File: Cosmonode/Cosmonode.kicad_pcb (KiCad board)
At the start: 2 copper layers, 59.7 x 34.9 mm, 30 parts, among them J1 CONN_01X07, J2 CONN_01X07, J3 CONN_01X02, J4 CONN_01X01, J5 CONN_01X06, SW1 SW_DIP_x01, U1 ATMEGA328P-AU, U2 RFM69CW, U3 M25P40, U4 XC6206P332MR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

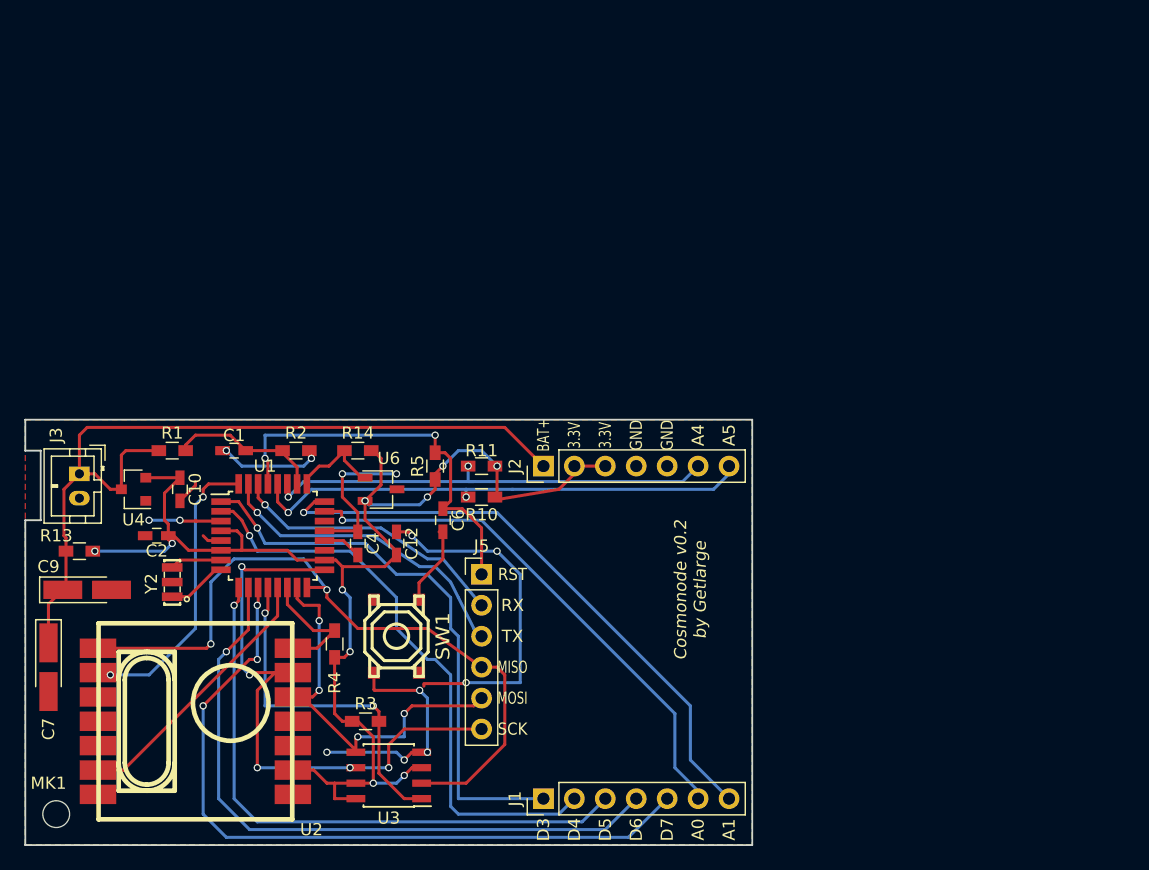
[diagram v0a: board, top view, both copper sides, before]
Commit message: new version 0.3
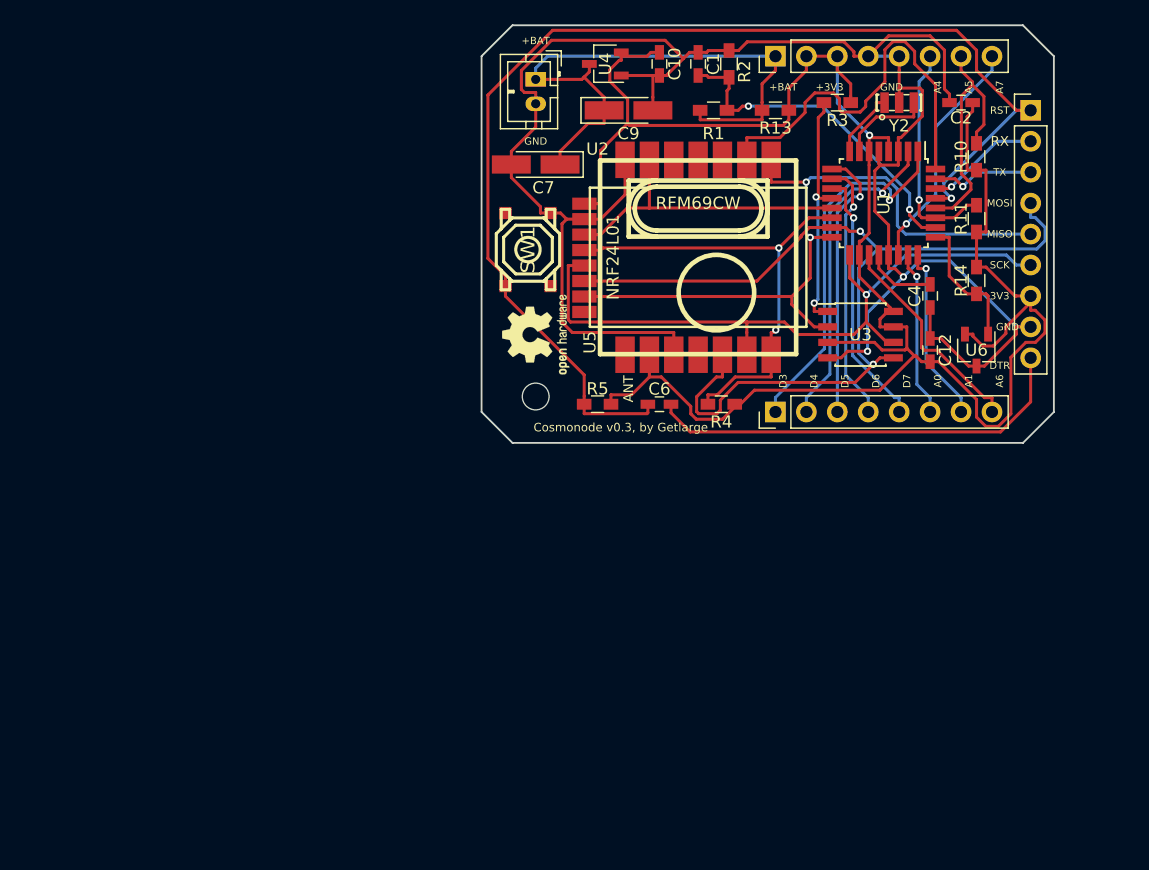
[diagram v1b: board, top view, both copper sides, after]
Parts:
- added U5: NRF24L01, mysensors_radios:NRF24L01-SMD, F.Cu at (163.2, 96.5)
- J1, J2: value CONN_01X07 -> CONN_01X08; footprint Socket_Strips:Socket_Strip_Straight_1x07_Pitch2.54mm -> Pin_Headers:Pin_Header_Straight_1x08_Pitch2.54mm
- J4: moved to F.Cu
- J5: value CONN_01X06 -> CONN_01X09; footprint Pin_Headers:Pin_Header_Straight_1x06_Pitch2.54mm -> Pin_Headers:Pin_Header_Straight_1x09_Pitch2.54mm
- U4: footprint TO_SOT_Packages_SMD:SOT-23 -> TO_SOT_Packages_SMD:TSOT-23
- moved C2 75.0 mm to (185.4, 83.8)
- moved Y2 71.5 mm to (180.3, 83.8), turned to 0 degrees
- moved R13 67.6 mm to (170.2, 84.5)
- moved R3 63.9 mm to (175.3, 83.8), turned to 180 degrees
- moved C9 59.4 mm to (158.1, 84.5)
- moved J5 59.0 mm to (191.1, 84.5)
- moved C7 57.5 mm to (150.5, 88.9), turned to 180 degrees
- moved U1 57.1 mm to (179.1, 92.1), turned to 270 degrees
- moved U2 56.2 mm to (163.8, 96.5), turned to 270 degrees
- moved U3 53.0 mm to (177.2, 102.9), turned to 0 degrees
- moved R14 52.7 mm to (186.7, 98.4), turned to 90 degrees
- moved C10 52.6 mm to (160.7, 80.6)
- moved R1 52.5 mm to (165.1, 84.5)
- moved MK1 52.2 mm to (150.5, 108.0)
- moved U4 52.2 mm to (156.2, 80.6)
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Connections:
- J5 pad 4: /MISO -> /MOSI
- J5 pad 5: /MOSI -> /MISO
- SW1 pad 2: /DTR -> /RST
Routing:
- net GND: track 79.8 -> 163.5 mm, vias 13 -> 2
- net /RST: track 33.0 -> 98.3 mm, vias 2 -> 1
- net +3V3: track 112.8 -> 170.1 mm, vias 10 -> 1
- net /MOSI: track 33.4 -> 79.7 mm, vias 4 -> 2
- net /D7: track 61.1 -> 21.6 mm, vias 3 -> 1
- net /A1: track 49.3 -> 14.8 mm
- net /D6: track 54.7 -> 21.6 mm
- net /A0: track 43.8 -> 13.7 mm
- net /DTR: track 6.70 -> 35.5 mm
- net /D10: track 10.2 -> 39.0 mm, vias 0 -> 2
- net /D5: track 49.6 -> 22.7 mm
- net /D4: track 48.8 -> 26.8 mm
- net /A5: track 41.8 -> 21.0 mm, vias 2 -> 0
- net /BAT+: track 67.9 -> 48.0 mm
- net /A7: track 0.00 -> 19.5 mm, vias 0 -> 1
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- removed copper zone on F.Cu, net GND
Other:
- board size 59.7 x 34.9 mm -> 47 x 34.3 mm
- board text added: "+3V3"
- board text added: "+BAT"
- board text added: "3V3"
- board text added: "A6"
- board text added: "A7"
- board text added: "ANT"
- board text added: "Cosmonode v0.3, by Getlarge"
- board text added: "DTR"
- board text added: "Do it yourself and do your best"
- board text removed: "3.3V"
- board text removed: "BAT+"
- board text removed: "Cosmonode v0.2 by Getlarge"

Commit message: big push!
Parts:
- removed C10: 4.7uF, Capacitors_SMD:C_0603_HandSoldering
- removed C12: 100nF, Capacitors_SMD:C_0603_HandSoldering
- removed C9: 47uF, Capacitors_Tantalum_SMD:CP_Tantalum_Case-A_EIA-3216-18_Hand
- removed R10, R11: 1k, Resistors_SMD:R_0603_HandSoldering
- removed R13: 0, Resistors_SMD:R_0603_HandSoldering
- removed R14: 100k, Resistors_SMD:R_0603_HandSoldering
- removed Y2: Crystal_GND2, SMD-RESONATOR-8MHZ-33PF-0.1__3P-3.2X1.3MM_:X3-SMD-3.6X1.3X0.8MM
- added C3: 100nF, Capacitors_SMD:C_0603_HandSoldering, F.Cu at (183.5, 100.3)
- added C5: 47uF, Capacitors_Tantalum_SMD:CP_Tantalum_Case-A_EIA-3216-18_Hand, F.Cu at (158.1, 85.1)
- added C8: 100nF, Capacitors_SMD:C_0603_HandSoldering, F.Cu at (188.0, 84.5)
- added J10: WEEE_Logo, Symbols:WEEE-Logo_4.2x6mm_SilkScreen, B.Cu at (184.2, 97.8)
- added J11: Aloes_Logo, Aloes:Aloes, B.Cu at (156.2, 100.3)
- added J12: Aloes_mini_Logo, Aloes:Aloes_mini, F.Cu at (149.9, 108.0)
- added J6: GS3, Connectors:GS3, F.Cu at (161.3, 109.2)
- added R6: 0, Resistors_SMD:R_0603_HandSoldering, F.Cu at (161.3, 80.6)
- added R7: 100k, Resistors_SMD:R_0603_HandSoldering, F.Cu at (187.3, 89.5)
- added R8: 1M, Resistors_SMD:R_0603_HandSoldering, F.Cu at (167.6, 85.1)
- added R9: 470k, Resistors_SMD:R_0603_HandSoldering, F.Cu at (164.5, 85.1)
- added Y1: Crystal_GND2, SMD-RESONATOR-8MHZ-33PF:X3-SMD-3.6X1.3X0.8MM, F.Cu at (177.8, 85.1)
- C4: value 100nF -> 47uF; footprint Capacitors_SMD:C_0603_HandSoldering -> Capacitors_Tantalum_SMD:CP_Tantalum_Case-A_EIA-3216-18_Hand
- C6: value 100nF -> 4.7uF
- C7: value 47uF -> 100nF; footprint Capacitors_Tantalum_SMD:CP_Tantalum_Case-A_EIA-3216-18_Hand -> Capacitors_SMD:C_0603_HandSoldering
- J3: value CONN_01X02 -> CONN_01X09; footprint Connectors_JST:JST_PH_B2B-PH-K_02x2.00mm_Straight -> Pin_Headers:Pin_Header_Straight_1x09_Pitch2.54mm
- J4: value CONN_01X01 -> OSHW; moved to B.Cu
- J5: value CONN_01X09 -> CONN_01X02; footprint Pin_Headers:Pin_Header_Straight_1x09_Pitch2.54mm -> Connectors_JST:JST_PH_B2B-PH-K_02x2.00mm_Straight
- R1: value 1M -> 10k
- R2: value 470k -> 10k
- R4, R5: value 10k -> 1k
- U3: value M25P40 -> NRF24L01_Breakout; footprint Housings_SOIC:SOIC-8_3.9x4.9mm_Pitch1.27mm -> mysensors_radios:NRF24L01-SMD
- U4: value XC6206P332MR -> M25P40; footprint TO_SOT_Packages_SMD:TSOT-23 -> Housings_SOIC:SOIC-8_3.9x4.9mm_Pitch1.27mm
- U5: value NRF24L01 -> XC6206P332MR; footprint mysensors_radios:NRF24L01-SMD -> TO_SOT_Packages_SMD:TSOT-23
- moved J3 41.4 mm to (191.8, 84.5), turned to 0 degrees
- moved J5 40.7 mm to (150.5, 81.9), turned to 270 degrees
- moved J4 36.4 mm to (184.2, 88.9), turned to 270 degrees
- moved R5 35.5 mm to (181.6, 84.5), turned to 90 degrees
- moved C4 33.5 mm to (151.1, 88.9), turned to 0 degrees
- moved R4 30.7 mm to (184.8, 84.5), turned to 90 degrees
- moved U4 30.5 mm to (177.2, 102.9), turned to 90 degrees
- moved C6 28.2 mm to (164.5, 80.6), turned to 270 degrees
- moved R2 28.0 mm to (181.6, 104.1), turned to 270 degrees
- moved R1 24.7 mm to (187.3, 95.2), turned to 270 degrees
- moved R3 20.4 mm to (187.3, 100.3), turned to 270 degrees
- moved C7 19.0 mm to (167.6, 80.6), turned to 270 degrees
- moved U5 17.1 mm to (156.8, 80.6), turned to 180 degrees
- moved U3 14.8 mm to (163.8, 96.5), turned to 270 degrees
- moved MK1 14.0 mm to (149.9, 94.0)
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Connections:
- C1 pad 1: GND -> +3V3
- C1 pad 2: /A3 -> GND
- C2 pad 1: +3V3 -> GND
- C2 pad 2: GND -> Net-(C2-Pad2)
- C4 pad 1: GND -> /BAT+
- C4 pad 2: Net-(C4-Pad2) -> GND
- C6 pad 1: /RST -> +3V3
- C6 pad 2: /DTR -> GND
- C7 pad 1: /BAT+ -> GND
- C7 pad 2: GND -> /A3
- J3 pad 1: /BAT+ -> /RST
- J3 pad 2: GND -> /RX
- J5 pad 1: /RST -> /BAT+
- J5 pad 2: /RX -> GND
- R1 pad 1: /BAT+ -> +3V3
- R1 pad 2: /A3 -> /D8
- R2 pad 1: /A3 -> +3V3
- R2 pad 2: GND -> /D10
- R3 pad 2: /D8 -> /RST
- R4 pad 2: /D10 -> /A5
- R5 pad 2: /RST -> /A4
- U1 pad 20: Net-(C4-Pad2) -> Net-(C2-Pad2)
- U2 pad 9: +3V3 -> /VCC_RFM69
- U3 pad 1: /D8 -> GND
- U3 pad 2: /MISO -> /VCC_NRF24
- U3 pad 3: +3V3 -> /D9
- U3 pad 4: GND -> /D10
- U3 pad 5: /MOSI -> /SCK
- U3 pad 6: /SCK -> /MOSI
- U3 pad 7: +3V3 -> /MISO
- U3 pad 8: +3V3 -> Net-(U3-Pad8)
- U4 pad 1: GND -> /D8
- U4 pad 2: +3V3 -> /MISO
- U4 pad 3: /BAT+ -> +3V3
- U5 pad 3: /D9 -> /BAT+
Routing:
- net /DTR: track 35.5 -> 0.00 mm
- net /VCC_NRF24: track 0.00 -> 23.9 mm
- net /D8: track 20.0 -> 39.5 mm, vias 2 -> 3
- net +3V3: track 170.1 -> 153.1 mm, vias 1 -> 0
- net Net-(C2-Pad2): track 0.00 -> 14.1 mm, vias 0 -> 2
- net GND: track 163.5 -> 177.6 mm, vias 2 -> 1
- net /D2: track 33.7 -> 20.7 mm, vias 0 -> 2
- net /D3: track 30.7 -> 40.6 mm
- net /A2: track 11.3 -> 20.6 mm
- net /SCK: track 58.0 -> 64.0 mm
- net Net-(C4-Pad2): track 5.88 -> 0.00 mm
- net /VCC_RFM69: track 0.00 -> 5.41 mm
- net /D10: track 39.0 -> 44.0 mm
- net /RST: track 98.3 -> 102.4 mm, vias 1 -> 2
- net /MISO: track 60.3 -> 56.7 mm, vias 2 -> 3
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- added copper zone on B.Cu, net GND
- added copper zone on F.Cu, net GND
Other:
- board text added: "ALOES.IO"
- board text added: "AREF"
- board text added: "Cosmonode v0.3, by Getlarge https://framagit.org/aloes"
- board text added: "NRF24"
- board text added: "RFM69"
- board text removed: "Cosmonode v0.3, by Getlarge"
- board text removed: "DTR"

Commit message: big push2
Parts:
- moved J3 0.64 mm to (191.1, 84.5)
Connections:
- C2 pad 2: Net-(C2-Pad2) -> /AREF
- J3 pad 9: GND -> /AREF
- U1 pad 20: Net-(C2-Pad2) -> /AREF
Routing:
- net /MISO: track 56.7 -> 91.3 mm, vias 3 -> 4
- net /AREF: track 0.00 -> 30.0 mm, vias 0 -> 2
- net /MOSI: track 77.2 -> 56.0 mm, vias 3 -> 2
- net Net-(C2-Pad2): track 14.1 -> 0.00 mm, vias 2 -> 0
- net /SCK: track 64.0 -> 76.7 mm, vias 1 -> 2
- net /D8: track 39.5 -> 27.2 mm, vias 3 -> 2
- net /D3: track 40.6 -> 33.1 mm
- net +3V3: track 153.1 -> 147.6 mm
- net /A3: track 29.4 -> 34.3 mm
- net /RST: track 102.4 -> 97.8 mm
- net /A6: track 16.8 -> 19.4 mm, vias 0 -> 1
- net /D10: track 44.0 -> 46.3 mm, vias 2 -> 0
- net /D2: track 20.7 -> 18.4 mm
- net /A2: track 20.6 -> 18.8 mm, vias 0 -> 2
- net GND: track 177.6 -> 178.6 mm
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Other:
- board text added: "ALOES"
- board text added: "Cosmonode v0.3, by Getlarge https://aloes.io https://framagit.org/aloes"
- board text removed: "Cosmonode v0.3, by Getlarge https://framagit.org/aloes"

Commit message: fix before test
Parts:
- added J7: Kicad_Logo, Symbols:KiCad-Logo2_6mm_SilkScreen, B.Cu at (183.5, 90.8)
- moved J4 16.8 mm to (175.9, 103.5)
- moved J10 5.75 mm to (183.5, 103.5)
